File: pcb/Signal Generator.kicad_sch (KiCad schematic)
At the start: 7 parts, among them J1 AudioJack3, J2 Conn_02x02_Odd_Even, J3 Screw_Terminal_01x04, J4 MEM2080-00-128-00-A

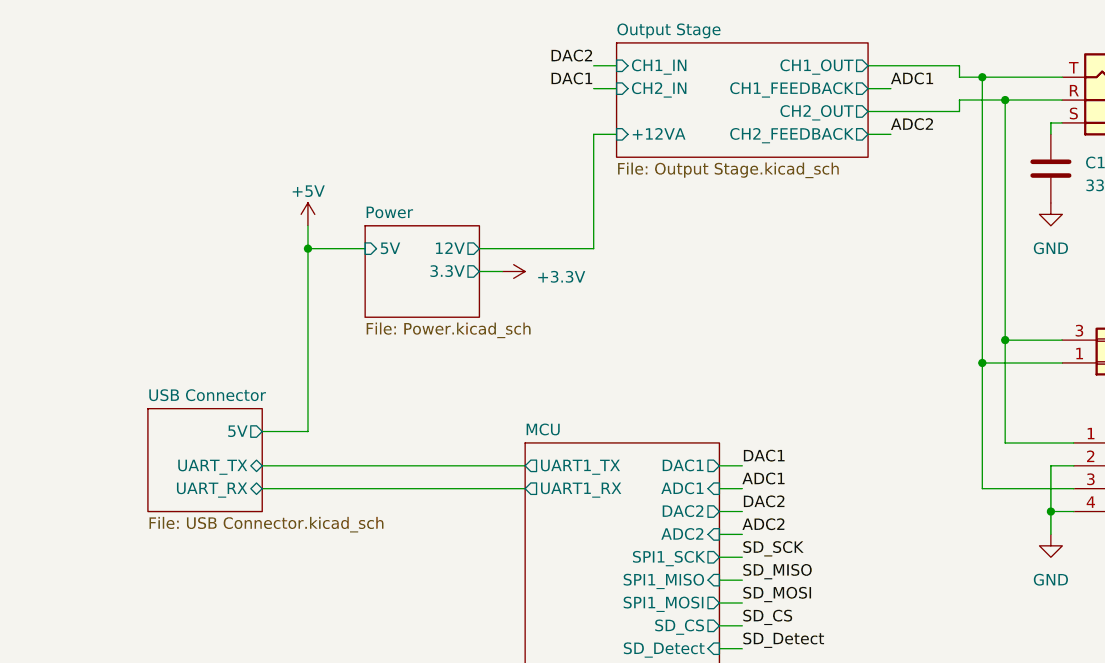
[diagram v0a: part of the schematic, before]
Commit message: Fixed FTDI connection to the stm32
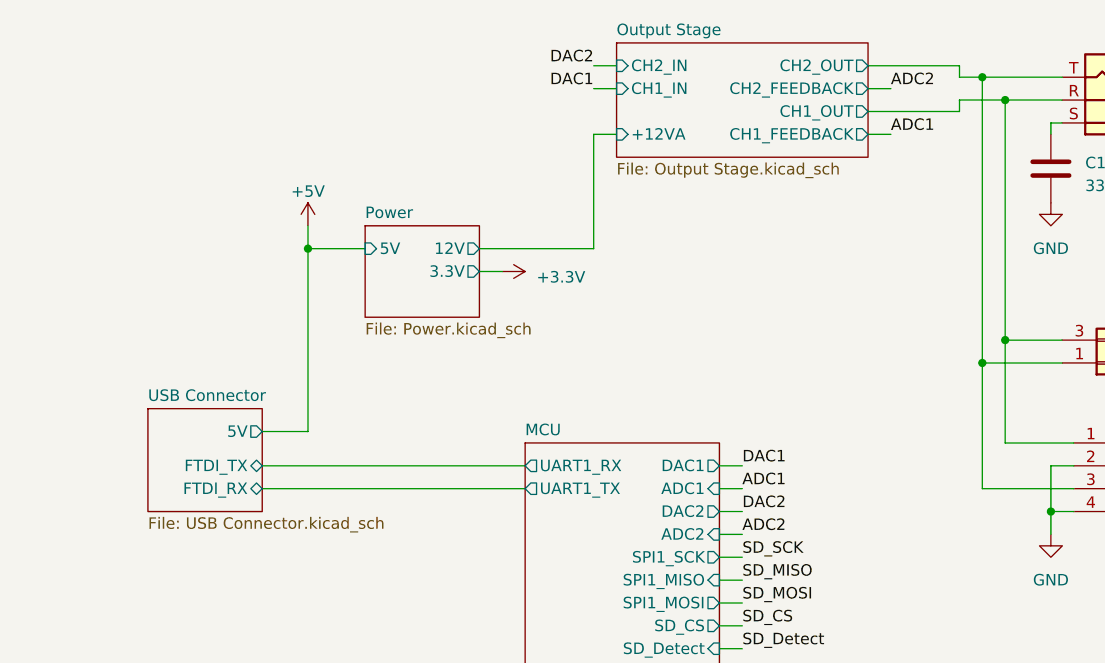
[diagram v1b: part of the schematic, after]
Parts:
- C1: PN (none) -> 10SVPC330M
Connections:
- net Output Stage/CH1_OUT: now also J1.R, J2.3 (Pin_3), J3.1 (Pin_1); no longer J1.T, J2.1 (Pin_1), J3.3 (Pin_3)
- net Output Stage/CH2_OUT: now also J1.T, J2.1 (Pin_1), J3.3 (Pin_3); no longer J1.R, J2.3 (Pin_3), J3.1 (Pin_1)
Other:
- sheet USB Connector ports: added FTDI_RX, FTDI_TX; removed UART_RX, UART_TX
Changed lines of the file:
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@@
+    (stroke (width 0) (type default))
+  )
+  (wire (pts (xy 179.07 92.71) (xy 179.07 97.79))
+    (stroke (width 0) (type default))
+  )
+  (wire (pts (xy 193.04 78.74) (xy 194.31 78.74))
+    (stroke (width 0) (type default))
+  )
+  (wire (pts (xy 179.07 55.88) (xy 179.07 54.61))
+    (stroke (width 0) (type default))
+  )
+  (wire (pts (xy 142.24 100.33) (xy 144.78 100.33))
     (stroke (width 0) (type default))
   )
@@
     (stroke (width 0) (type default))
   )
-  (wire (pts (xy 179.07 92.71) (xy 179.07 97.79))
-    (stroke (width 0) (type default))
-  )
-  (wire (pts (xy 193.04 78.74) (xy 194.31 78.74))
-    (stroke (width 0) (type default))
-  )
-  (wire (pts (xy 179.07 55.88) (xy 179.07 54.61))
-    (stroke (width 0) (type default))
-  )
-  (wire (pts (xy 142.24 100.33) (xy 144.78 100.33))
-    (stroke (width 0) (type default))
-  )
   (wire (pts (xy 115.57 71.12) (xy 118.11 71.12))
     (stroke (width 0) (type default))
   )
+  (wire (pts (xy 194.31 78.74) (xy 194.31 81.28))
+    (stroke (width 0) (type default))
+  )
+  (wire (pts (xy 171.45 165.1) (xy 171.45 167.64))
+    (stroke (width 0) (type default))
+  )
+  (wire (pts (xy 142.24 97.79) (xy 144.78 97.79))
+    (stroke (width 0) (type default))
+  )
+  (wire (pts (xy 158.75 50.8) (xy 161.29 50.8))
+    (stroke (width 0) (type default))
+  )
+  (wire (pts (xy 142.24 107.95) (xy 144.78 107.95))
+    (stroke (width 0) (type default))
+  )
+  (wire (pts (xy 189.23 157.48) (xy 189.23 165.1))
+    (stroke (width 0) (type default))
+  )
+  (wire (pts (xy 204.47 167.64) (xy 207.01 167.64))
+    (stroke (width 0) (type default))
+  )
+  (wire (pts (xy 171.45 152.4) (xy 171.45 154.94))
+    (stroke (width 0) (type default))
+  )
+  (wire (pts (xy 173.99 90.17) (xy 173.99 78.74))
+    (stroke (width 0) (type default))
+  )
+  (wire (pts (xy 168.91 49.53) (xy 171.45 49.53))
+    (stroke (width 0) (type default))
+  )
+  (wire (pts (xy 171.45 95.25) (xy 171.45 81.28))
+    (stroke (width 0) (type default))
+  )
+  (wire (pts (xy 204.47 160.02) (xy 209.55 160.02))
+    (stroke (width 0) (type default))
+  )
+  (wire (pts (xy 181.61 92.71) (xy 179.07 92.71))
+    (stroke (width 0) (type default))
+  )
+  (wire (pts (xy 142.24 92.71) (xy 144.78 92.71))
+    (stroke (width 0) (type default))
+  )
+  (wire (pts (xy 168.91 52.07) (xy 173.99 52.07))
+    (stroke (width 0) (type default))
+  )
+  (wire (pts (xy 179.07 97.79) (xy 181.61 97.79))
+    (stroke (width 0) (type default))
+  )
+  (wire (pts (xy 96.52 68.58) (xy 96.52 88.9))
+    (stroke (width 0) (type default))
+  )
+  (wire (pts (xy 171.45 49.53) (xy 180.34 49.53))
+    (stroke (width 0) (type default))
+  )
+  (wire (pts (xy 96.52 66.04) (xy 96.52 68.58))
+    (stroke (width 0) (type default))
+  )
+  (wire (pts (xy 142.24 102.87) (xy 144.78 102.87))
+    (stroke (width 0) (type default))
+  )
+  (wire (pts (xy 171.45 49.53) (xy 171.45 81.28))
+    (stroke (width 0) (type default))
+  )
+  (wire (pts (xy 180.34 81.28) (xy 171.45 81.28))
+    (stroke (width 0) (type default))
+  )
+  (wire (pts (xy 128.27 48.26) (xy 130.81 48.26))
+    (stroke (width 0) (type default))
+  )
+  (wire (pts (xy 173.99 52.07) (xy 173.99 78.74))
+    (stroke (width 0) (type default))
+  )
+  (wire (pts (xy 179.07 54.61) (xy 180.34 54.61))
+    (stroke (width 0) (type default))
+  )
+  (wire (pts (xy 142.24 113.03) (xy 144.78 113.03))
+    (stroke (width 0) (type default))
+  )
+  (wire (pts (xy 204.47 154.94) (xy 209.55 154.94))
+    (stroke (width 0) (type default))
+  )
+  (wire (pts (xy 171.45 165.1) (xy 182.88 165.1))
+    (stroke (width 0) (type default))
+  )
+  (wire (pts (xy 204.47 149.86) (xy 209.55 149.86))
+    (stroke (width 0) (type default))
+  )
   (wire (pts (xy 91.44 92.71) (xy 120.65 92.71))
-    (stroke (width 0) (type default))
-  )
-  (wire (pts (xy 194.31 78.74) (xy 194.31 81.28))
-    (stroke (width 0) (type default))
-  )
-  (wire (pts (xy 171.45 165.1) (xy 171.45 167.64))
-    (stroke (width 0) (type default))
-  )
-  (wire (pts (xy 142.24 97.79) (xy 144.78 97.79))
-    (stroke (width 0) (type default))
-  )
-  (wire (pts (xy 158.75 50.8) (xy 161.29 50.8))
-    (stroke (width 0) (type default))
-  )
-  (wire (pts (xy 142.24 107.95) (xy 144.78 107.95))
-    (stroke (width 0) (type default))
-  )
-  (wire (pts (xy 189.23 157.48) (xy 189.23 165.1))
-    (stroke (width 0) (type default))
-  )
-  (wire (pts (xy 204.47 167.64) (xy 207.01 167.64))
-    (stroke (width 0) (type default))
-  )
-  (wire (pts (xy 171.45 152.4) (xy 171.45 154.94))
-    (stroke (width 0) (type default))
-  )
-  (wire (pts (xy 173.99 90.17) (xy 173.99 78.74))
-    (stroke (width 0) (type default))
-  )
-  (wire (pts (xy 168.91 49.53) (xy 171.45 49.53))
-    (stroke (width 0) (type default))
-  )
-  (wire (pts (xy 171.45 95.25) (xy 171.45 81.28))
-    (stroke (width 0) (type default))
-  )
-  (wire (pts (xy 204.47 160.02) (xy 209.55 160.02))
-    (stroke (width 0) (type default))
-  )
-  (wire (pts (xy 181.61 92.71) (xy 179.07 92.71))
-    (stroke (width 0) (type default))
-  )
-  (wire (pts (xy 142.24 92.71) (xy 144.78 92.71))
-    (stroke (width 0) (type default))
-  )
-  (wire (pts (xy 168.91 52.07) (xy 173.99 52.07))
-    (stroke (width 0) (type default))
-  )
-  (wire (pts (xy 179.07 97.79) (xy 181.61 97.79))
-    (stroke (width 0) (type default))
-  )
-  (wire (pts (xy 96.52 68.58) (xy 96.52 88.9))
-    (stroke (width 0) (type default))
-  )
-  (wire (pts (xy 171.45 49.53) (xy 180.34 49.53))
-    (stroke (width 0) (type default))
-  )
-  (wire (pts (xy 96.52 66.04) (xy 96.52 68.58))
-    (stroke (width 0) (type default))
-  )
-  (wire (pts (xy 142.24 102.87) (xy 144.78 102.87))
-    (stroke (width 0) (type default))
-  )
-  (wire (pts (xy 171.45 49.53) (xy 171.45 81.28))
-    (stroke (width 0) (type default))
-  )
-  (wire (pts (xy 180.34 81.28) (xy 171.45 81.28))
-    (stroke (width 0) (type default))
-  )
-  (wire (pts (xy 128.27 48.26) (xy 130.81 48.26))
-    (stroke (width 0) (type default))
-  )
-  (wire (pts (xy 173.99 52.07) (xy 173.99 78.74))
-    (stroke (width 0) (type default))
-  )
-  (wire (pts (xy 179.07 54.61) (xy 180.34 54.61))
-    (stroke (width 0) (type default))
-  )
-  (wire (pts (xy 142.24 113.03) (xy 144.78 113.03))
-    (stroke (width 0) (type default))
-  )
-  (wire (pts (xy 204.47 154.94) (xy 209.55 154.94))
-    (stroke (width 0) (type default))
-  )
-  (wire (pts (xy 171.45 165.1) (xy 182.88 165.1))
-    (stroke (width 0) (type default))
-  )
-  (wire (pts (xy 204.47 149.86) (xy 209.55 149.86))
     (stroke (width 0) (type default))
   )
@@
     (effects (font (size 1.27 1.27)) (justify right bottom))
   )
-  (label "ADC2" (at 161.29 55.88 0) (fields_autoplaced)
-    (effects (font (size 1.27 1.27)) (justify left bottom))
-  )
-  (label "ADC1" (at 161.29 50.8 0) (fields_autoplaced)
+  (label "ADC1" (at 161.29 55.88 0) (fields_autoplaced)
+    (effects (font (size 1.27 1.27)) (justify left bottom))
+  )
+  (label "ADC2" (at 161.29 50.8 0) (fields_autoplaced)
     (effects (font (size 1.27 1.27)) (justify left bottom))
   )
@@
       (effects (font (size 1.27 1.27)) hide)
     )
+    (property "PN" "10SVPC330M" (at 179.07 59.69 0)
+      (effects (font (size 1.27 1.27)) hide)
+    )
     (pin "1")
     (pin "2")
@@
       (effects (font (size 1.27 1.27)) (justify right))
     )
-    (pin "UART_TX" bidirectional (at 91.44 92.71 0)
-      (effects (font (size 1.27 1.27)) (justify right))
-    )
-    (pin "UART_RX" bidirectional (at 91.44 95.25 0)
+    (pin "FTDI_TX" bidirectional (at 91.44 92.71 0)
+      (effects (font (size 1.27 1.27)) (justify right))
+    )
+    (pin "FTDI_RX" bidirectional (at 91.44 95.25 0)
       (effects (font (size 1.27 1.27)) (justify right))
     )
@@
       (effects (font (size 1.27 1.27)) (justify left top))
     )
-    (pin "CH1_OUT" output (at 158.75 48.26 0)
-      (effects (font (size 1.27 1.27)) (justify right))
-    )
-    (pin "CH1_FEEDBACK" output (at 158.75 50.8 0)
-      (effects (font (size 1.27 1.27)) (justify right))
-    )
-    (pin "CH1_IN" input (at 130.81 48.26 180)
-      (effects (font (size 1.27 1.27)) (justify left))
-    )
-    (pin "CH2_FEEDBACK" output (at 158.75 55.88 0)
-      (effects (font (size 1.27 1.27)) (justify right))
-    )
-    (pin "CH2_OUT" output (at 158.75 53.34 0)
-      (effects (font (size 1.27 1.27)) (justify right))
-    )
-    (pin "CH2_IN" input (at 130.81 50.8 180)
+    (pin "CH2_OUT" output (at 158.75 48.26 0)
+      (effects (font (size 1.27 1.27)) (justify right))
+    )
+    (pin "CH2_FEEDBACK" output (at 158.75 50.8 0)
+      (effects (font (size 1.27 1.27)) (justify right))
+    )
+    (pin "CH2_IN" input (at 130.81 48.26 180)
+      (effects (font (size 1.27 1.27)) (justify left))
+    )
+    (pin "CH1_FEEDBACK" output (at 158.75 55.88 0)
+      (effects (font (size 1.27 1.27)) (justify right))
+    )
+    (pin "CH1_OUT" output (at 158.75 53.34 0)
+      (effects (font (size 1.27 1.27)) (justify right))
+    )
+    (pin "CH1_IN" input (at 130.81 50.8 180)
       (effects (font (size 1.27 1.27)) (justify left))
     )
@@
       (effects (font (size 1.27 1.27)) (justify left top))
     )
-    (pin "UART1_TX" output (at 120.65 92.71 180)
-      (effects (font (size 1.27 1.27)) (justify left))
-    )
-    (pin "UART1_RX" output (at 120.65 95.25 180)
-      (effects (font (size 1.27 1.27)) (justify left))
-    )
+    (pin "UART1_TX" output (at 120.65 95.25 180)
+      (effects (font (size 1.27 1.27)) (justify left))
+    )
+    (pin "UART1_RX" output (at 120.65 92.71 180)
+      (effects (font (size 1.27 1.27)) (justify left))
+    )

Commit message: Switch to stm32f205
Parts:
- renumbered C2 to C1, C1 to C2
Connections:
- net SD_D2: now reaches J4.P1 (DAT2)
- net SD_D1: now reaches J4.P8 (DAT1)
- net SD_CS renamed SD_D3
- net SD_MISO renamed SD_D0
- net SD_MOSI renamed SD_CMD
- no-connect marks 2 -> 0
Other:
- sheet MCU ports: added SD_CMD, SD_D0, SD_D1, SD_D2, SD_D3, SD_SCK; removed SD_CS, SPI1_MISO, SPI1_MOSI, SPI1_SCK
